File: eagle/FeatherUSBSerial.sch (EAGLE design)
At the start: 14 parts, among them U1 FT232RLSSOP

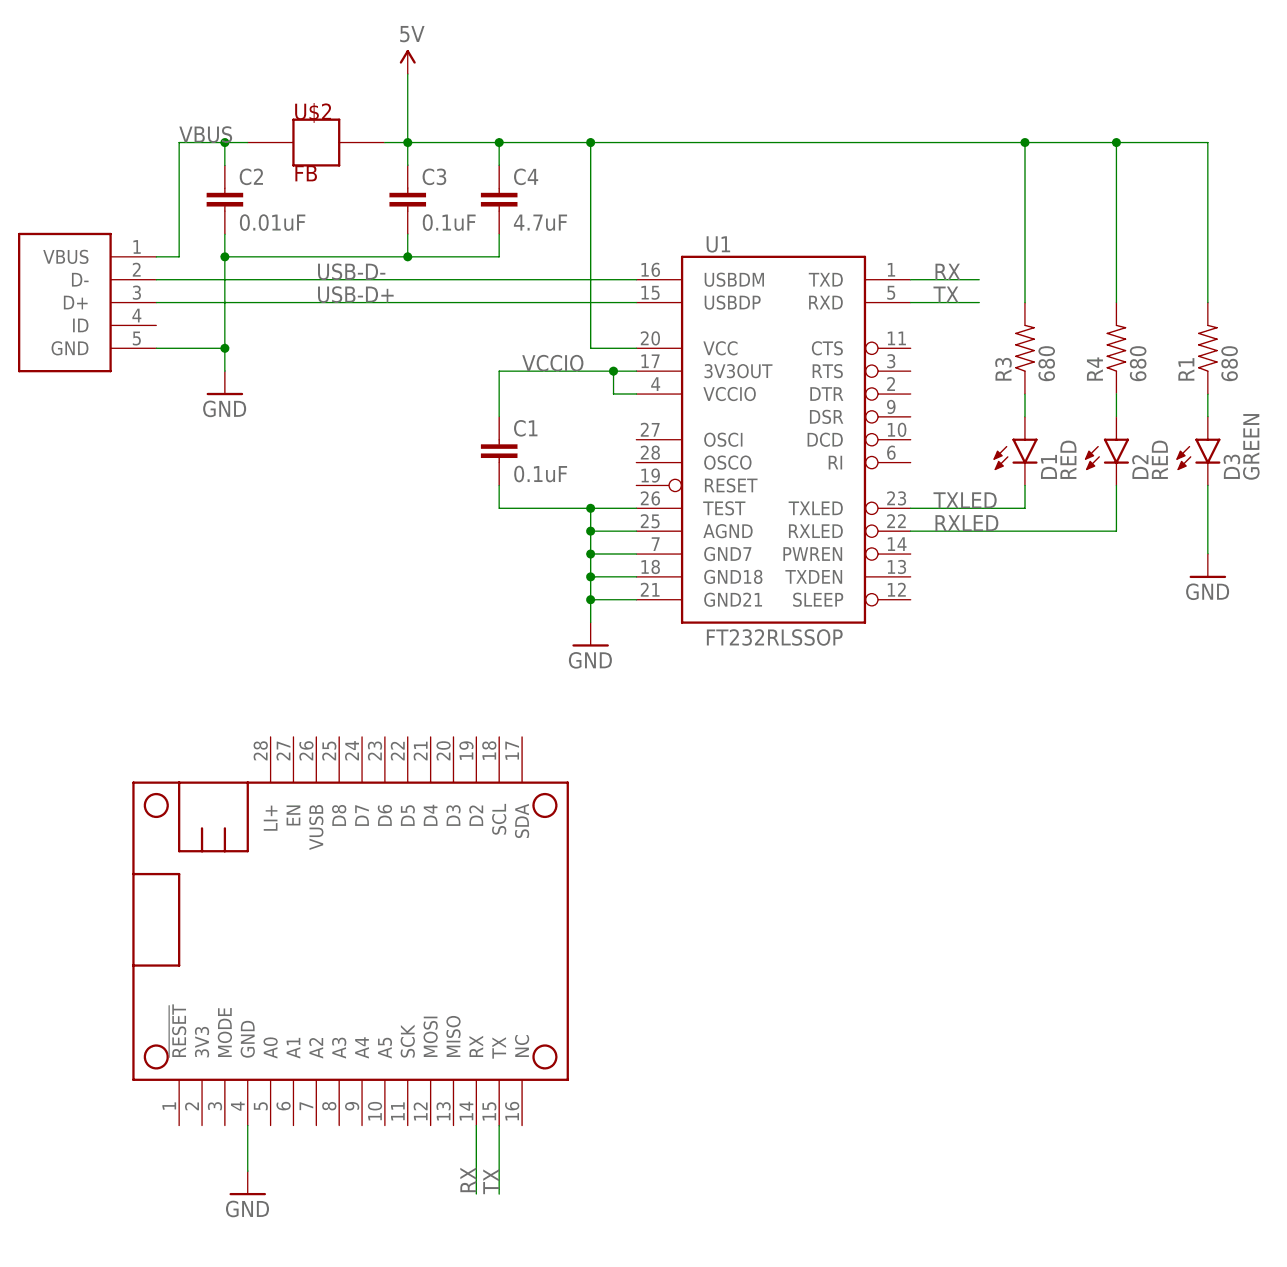
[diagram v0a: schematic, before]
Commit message: Added Big Buttons
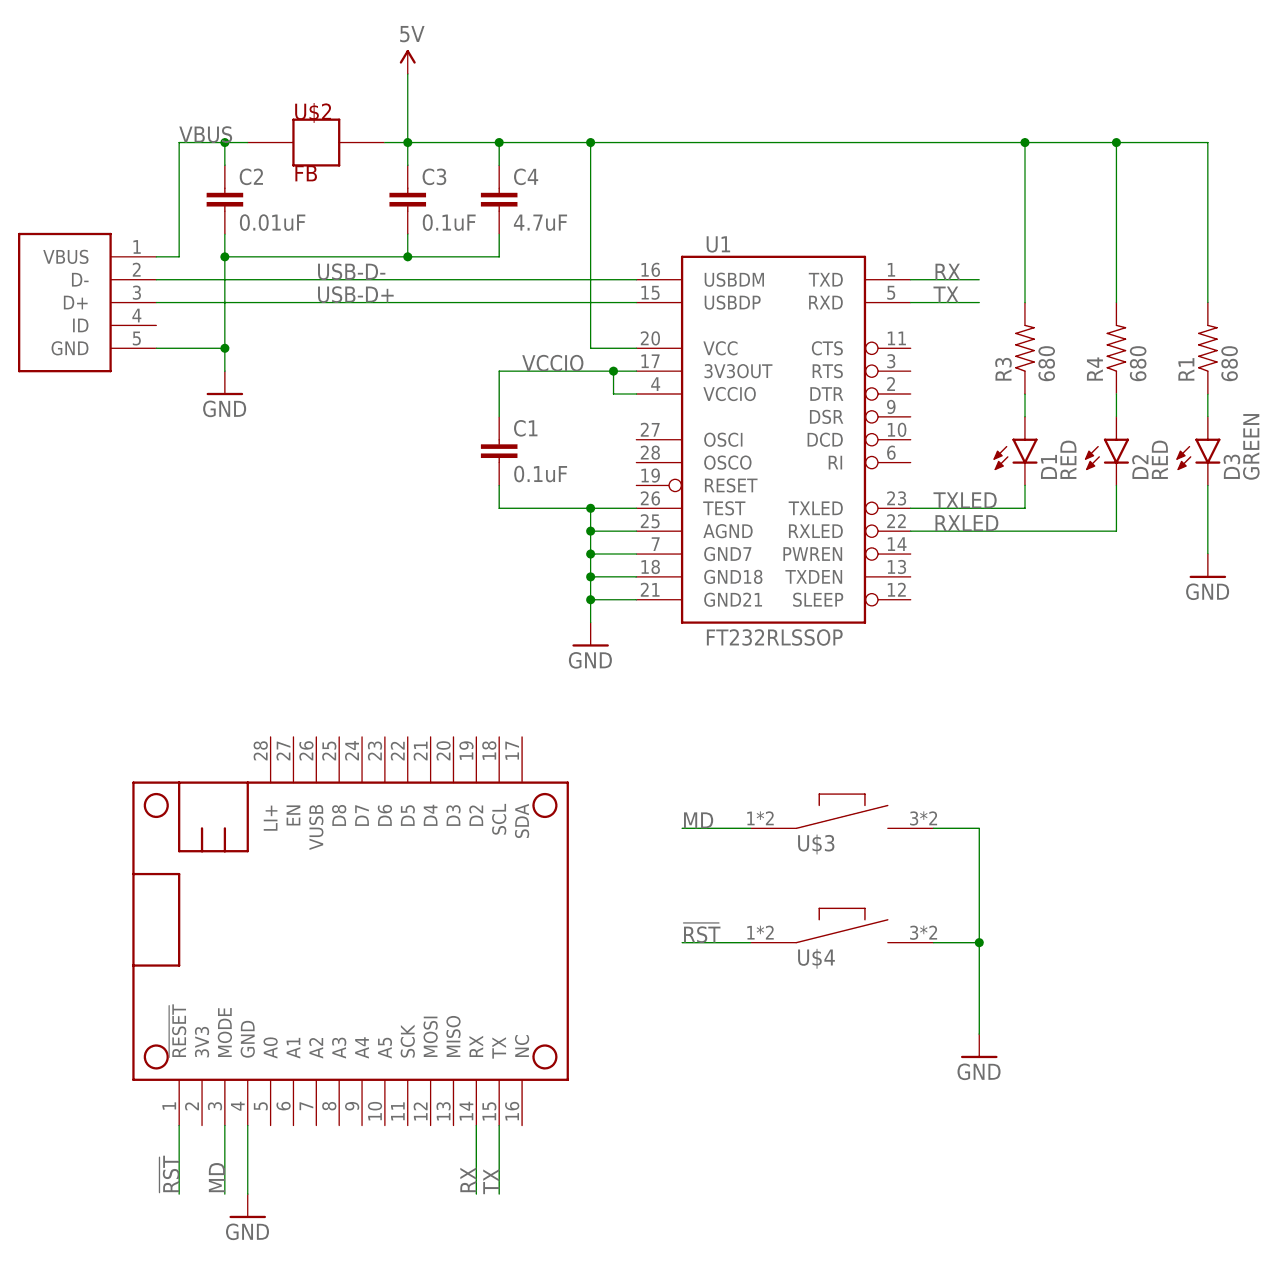
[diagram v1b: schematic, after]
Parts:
- added U$3, U$4: TL3300CFXXXQ, S2JLibrary:TL3300CFXXXQ
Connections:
- new net !RST: MS1.!RESET, U$4.P$1
- new net MD: MS1.MODE, U$3.P$1
- net GND: now also U$3.P$2, U$4.P$2
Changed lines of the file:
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@@
 <?xml version="1.0" encoding="utf-8"?>
 <!DOCTYPE eagle SYSTEM "eagle.dtd">
-<eagle version="9.2.2">
+<eagle version="9.3.0">
 <drawing>
 <settings>
@@
 <part name="R1" library="rickk2" deviceset="RES-680-0805" device="" value="680"/>
 <part name="GND4" library="rickk2" deviceset="GND" device=""/>
+<part name="U$3" library="S2JLibrary" deviceset="TL3300CFXXXQ" device=""/>
+<part name="U$4" library="S2JLibrary" deviceset="TL3300CFXXXQ" device=""/>
+<part name="GND5" library="rickk2" deviceset="GND" device=""/>
 </parts>
 <sheets>
@@
 <attribute name="VALUE" x="99.06" y="116.84" size="1.778" layer="96"/>
 </instance>
-<instance part="GND2" gate="1" x="104.14" y="30.48" smashed="yes">
-<attribute name="VALUE" x="101.6" y="27.94" size="1.778" layer="96"/>
+<instance part="GND2" gate="1" x="104.14" y="27.94" smashed="yes">
+<attribute name="VALUE" x="101.6" y="25.4" size="1.778" layer="96"/>
 </instance>
 <instance part="R3" gate="G$1" x="190.5" y="124.46" smashed="yes" rot="R90">
@@
 <instance part="GND4" gate="1" x="210.82" y="99.06" smashed="yes">
 <attribute name="VALUE" x="208.28" y="96.52" size="1.778" layer="96"/>
+</instance>
+<instance part="U$3" gate="G$1" x="170.18" y="71.12" smashed="yes">
+<attribute name="NAME" x="165.1" y="68.58" size="1.778" layer="95"/>
+</instance>
+<instance part="U$4" gate="G$1" x="170.18" y="58.42" smashed="yes">
+<attribute name="NAME" x="165.1" y="55.88" size="1.778" layer="95"/>
+</instance>
+<instance part="GND5" gate="1" x="185.42" y="45.72" smashed="yes">
+<attribute name="VALUE" x="182.88" y="43.18" size="1.778" layer="96"/>
 </instance>
 </instances>
@@
 <pinref part="MS1" gate="G$1" pin="GND"/>
 <pinref part="GND2" gate="1" pin="GND"/>
-<wire x1="104.14" y1="38.1" x2="104.14" y2="33.02" width="0.1524" layer="91"/>
+<wire x1="104.14" y1="38.1" x2="104.14" y2="30.48" width="0.1524" layer="91"/>
 </segment>
 <segment>
@@
 <wire x1="210.82" y1="109.22" x2="210.82" y2="101.6" width="0.1524" layer="91"/>
 <pinref part="GND4" gate="1" pin="GND"/>
+</segment>
+<segment>
+<pinref part="U$3" gate="G$1" pin="P$2"/>
+<wire x1="180.34" y1="71.12" x2="185.42" y2="71.12" width="0.1524" layer="91"/>
+<wire x1="185.42" y1="71.12" x2="185.42" y2="58.42" width="0.1524" layer="91"/>
+<pinref part="U$4" gate="G$1" pin="P$2"/>
+<wire x1="185.42" y1="58.42" x2="185.42" y2="48.26" width="0.1524" layer="91"/>
+<wire x1="180.34" y1="58.42" x2="185.42" y2="58.42" width="0.1524" layer="91"/>
+<junction x="185.42" y="58.42"/>
+<pinref part="GND5" gate="1" pin="GND"/>
 </segment>
 </net>
@@
 </segment>
 </net>
+<net name="MD" class="0">
+<segment>
+<pinref part="U$3" gate="G$1" pin="P$1"/>
+<wire x1="160.02" y1="71.12" x2="152.4" y2="71.12" width="0.1524" layer="91"/>
+<label x="152.4" y="71.12" size="1.778" layer="95"/>
+</segment>
+<segment>
+<pinref part="MS1" gate="G$1" pin="MODE"/>
+<wire x1="101.6" y1="38.1" x2="101.6" y2="30.48" width="0.1524" layer="91"/>
+<label x="101.6" y="30.48" size="1.778" layer="95" rot="R90"/>
+</segment>
+</net>
+<net name="!RST" class="0">
+<segment>
+<pinref part="U$4" gate="G$1" pin="P$1"/>
+<wire x1="160.02" y1="58.42" x2="152.4" y2="58.42" width="0.1524" layer="91"/>
+<label x="152.4" y="58.42" size="1.778" layer="95"/>
+</segment>
+<segment>
+<pinref part="MS1" gate="G$1" pin="!RESET"/>
+<wire x1="96.52" y1="38.1" x2="96.52" y2="30.48" width="0.1524" layer="91"/>
+<label x="96.52" y="30.48" size="1.778" layer="95" rot="R90"/>
+</segment>
+</net>

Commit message: Updated to use more common and easier to manipulate 0805 Cap's and Resistors.
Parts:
- C1, C3: device rickk2:CAP-0.1UF-0603 -> S2JLibrary:CAP_CERAMIC_0805MP
- C2: device rickk2:CAP-0.01UF-0603 -> S2JLibrary:CAP_CERAMIC_0805MP
- C4: device rickk2:CAP-4.7UF-0603 -> S2JLibrary:CAP_CERAMIC_0805MP
- R1, R3, R4: device rickk2:RES-680-0805 -> S2JLibrary:RESISTOR0805_NOOUTLINE
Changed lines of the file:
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@@
 <part name="D2" library="rickk2" deviceset="LED-RED" device="" value="RED"/>
 <part name="U$2" library="rickk2" deviceset="FERRITE-BEAD-MI0805K400R-10" device="" value="FB"/>
-<part name="C1" library="rickk2" deviceset="CAP-0.1UF-0603" device="" value="0.1uF"/>
-<part name="C2" library="rickk2" deviceset="CAP-0.01UF-0603" device="" value="0.01uF"/>
-<part name="C3" library="rickk2" deviceset="CAP-0.1UF-0603" device="" value="0.1uF"/>
-<part name="C4" library="rickk2" deviceset="CAP-4.7UF-0603" device="" value="4.7uF"/>
+<part name="C1" library="S2JLibrary" deviceset="CAP_CERAMIC" device="_0805MP" value="0.1uF"/>
+<part name="C2" library="S2JLibrary" deviceset="CAP_CERAMIC" device="_0805MP" value="0.01uF"/>
+<part name="C3" library="S2JLibrary" deviceset="CAP_CERAMIC" device="_0805MP" value="0.1uF"/>
+<part name="C4" library="S2JLibrary" deviceset="CAP_CERAMIC" device="_0805MP" value="4.7uF"/>
 <part name="GND1" library="rickk2" deviceset="GND" device=""/>
 <part name="GND2" library="rickk2" deviceset="GND" device=""/>
-<part name="R3" library="rickk2" deviceset="RES-680-0805" device="" value="680"/>
-<part name="R4" library="rickk2" deviceset="RES-680-0805" device="" value="680"/>
+<part name="R3" library="S2JLibrary" deviceset="RESISTOR" device="0805_NOOUTLINE" value="680"/>
+<part name="R4" library="S2JLibrary" deviceset="RESISTOR" device="0805_NOOUTLINE" value="680"/>
 <part name="SUPPLY1" library="rickk2" deviceset="5V" device=""/>
 <part name="GND3" library="rickk2" deviceset="GND" device=""/>
 <part name="D3" library="rickk2" deviceset="LED-GREEN" device="0603" value="GREEN"/>
-<part name="R1" library="rickk2" deviceset="RES-680-0805" device="" value="680"/>
+<part name="R1" library="S2JLibrary" deviceset="RESISTOR" device="0805_NOOUTLINE" value="680"/>
 <part name="GND4" library="rickk2" deviceset="GND" device=""/>
 <part name="U$3" library="S2JLibrary" deviceset="TL3300CFXXXQ" device=""/>
@@
 <instance part="C1" gate="G$1" x="132.08" y="111.76" smashed="yes">
 <attribute name="NAME" x="133.604" y="114.681" size="1.778" layer="95"/>
-<attribute name="VALUE" x="133.604" y="109.601" size="1.778" layer="96"/>
 </instance>
 <instance part="C2" gate="G$1" x="101.6" y="139.7" smashed="yes">
 <attribute name="NAME" x="103.124" y="142.621" size="1.778" layer="95"/>
-<attribute name="VALUE" x="103.124" y="137.541" size="1.778" layer="96"/>
 </instance>
 <instance part="C3" gate="G$1" x="121.92" y="139.7" smashed="yes">
 <attribute name="NAME" x="123.444" y="142.621" size="1.778" layer="95"/>
-<attribute name="VALUE" x="123.444" y="137.541" size="1.778" layer="96"/>
 </instance>
 <instance part="C4" gate="G$1" x="132.08" y="139.7" smashed="yes">
 <attribute name="NAME" x="133.604" y="142.621" size="1.778" layer="95"/>
-<attribute name="VALUE" x="133.604" y="137.541" size="1.778" layer="96"/>
 </instance>
 <instance part="GND1" gate="1" x="101.6" y="119.38" smashed="yes">
@@
 <instance part="R3" gate="G$1" x="190.5" y="124.46" smashed="yes" rot="R90">
 <attribute name="NAME" x="189.0014" y="120.65" size="1.778" layer="95" rot="R90"/>
-<attribute name="VALUE" x="193.802" y="120.65" size="1.778" layer="96" rot="R90"/>
 </instance>
 <instance part="R4" gate="G$1" x="200.66" y="124.46" smashed="yes" rot="R90">
 <attribute name="NAME" x="199.1614" y="120.65" size="1.778" layer="95" rot="R90"/>
-<attribute name="VALUE" x="203.962" y="120.65" size="1.778" layer="96" rot="R90"/>
 </instance>
 <instance part="SUPPLY1" gate="G$1" x="121.92" y="154.94" smashed="yes">
@@
 <instance part="R1" gate="G$1" x="210.82" y="124.46" smashed="yes" rot="R90">
 <attribute name="NAME" x="209.3214" y="120.65" size="1.778" layer="95" rot="R90"/>
-<attribute name="VALUE" x="214.122" y="120.65" size="1.778" layer="96" rot="R90"/>
 </instance>
 <instance part="GND4" gate="1" x="210.82" y="99.06" smashed="yes">
